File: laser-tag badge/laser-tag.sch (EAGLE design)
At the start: 47 parts, among them J1 JUMPER_SOLDER_1X2_CLOSED, J2 JUMPER_SOLDER_1X2_OPEN, J3 JUMPER_SOLDER_1X2_CLOSED, J4 JUMPER_SOLDER_1X2_CLOSED, J5 JUMPER_SOLDER_1X2_CLOSED, P1 E1260CS021, U1 MKL27Z256VLH4

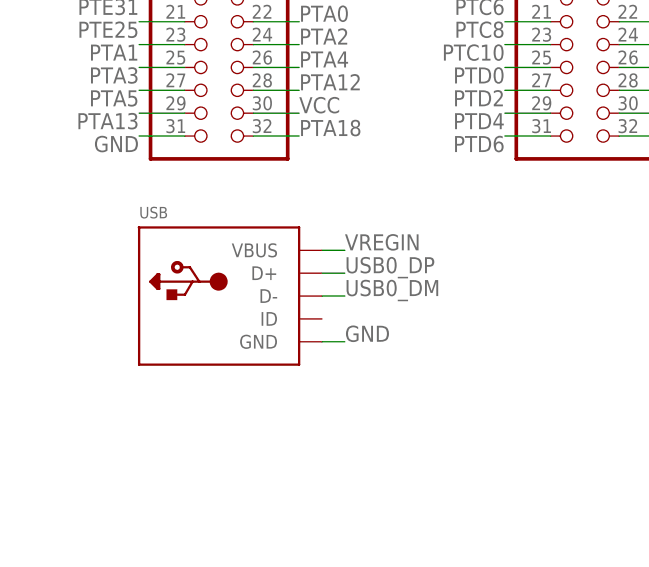
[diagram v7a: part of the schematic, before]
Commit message: Switch to micro-USB connector
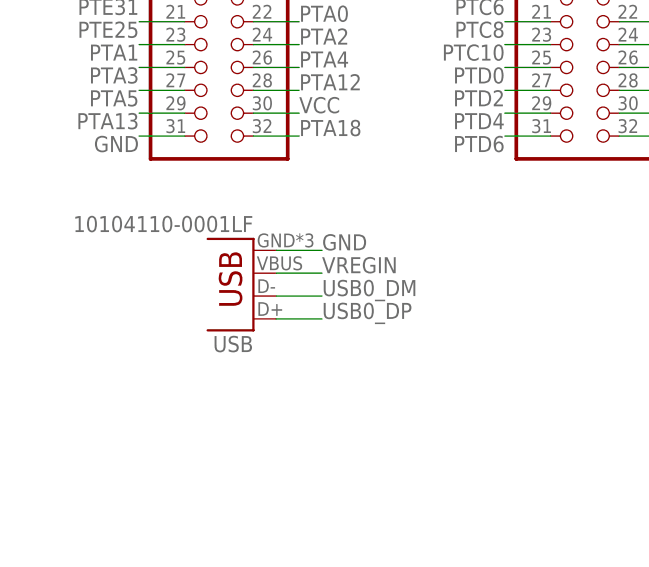
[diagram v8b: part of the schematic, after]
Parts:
- USB: value (none) -> 10104110-0001LF; device adafruit:USBMINIB -> SparkFun-Connectors:USB-MICROB
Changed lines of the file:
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@@
 <layer number="112" name="tSilk" color="7" fill="1" visible="no" active="yes"/>
 <layer number="113" name="ReferenceLS" color="7" fill="1" visible="no" active="no"/>
+<layer number="114" name="Badge_Outline" color="7" fill="1" visible="yes" active="yes"/>
+<layer number="115" name="ReferenceISLANDS" color="7" fill="1" visible="yes" active="yes"/>
 <layer number="116" name="Patch_BOT" color="9" fill="4" visible="no" active="yes"/>
 <layer number="118" name="Rect_Pads" color="7" fill="1" visible="no" active="no"/>
@@
 <part name="R1" library="rcl" deviceset="R-EU_" device="R0603" value="10k"/>
 <part name="GND2" library="supply1" deviceset="GND" device=""/>
-<part name="USB" library="adafruit" deviceset="USB" device="MINIB"/>
 <part name="R2" library="rcl" deviceset="R-EU_" device="R0603" value="10"/>
 <part name="C5" library="rcl" deviceset="C-EU" device="C0603K" value="10 uF"/>
@@
 <part name="R4" library="rcl" deviceset="R-EU_" device="R0603" value="10k"/>
 <part name="BAT2" library="adafruit" deviceset="CR2032" device="SMT" value="BK-883"/>
+<part name="USB" library="SparkFun-Connectors" deviceset="USB" device="-MICROB" value="10104110-0001LF"/>
 </parts>
 <sheets>
@@
 <instance part="R1" gate="G$1" x="-38.1" y="78.74" rot="R90"/>
 <instance part="GND2" gate="1" x="-38.1" y="68.58"/>
-<instance part="USB" gate="G$1" x="-106.68" y="5.08"/>
 <instance part="R2" gate="G$1" x="-17.78" y="86.36" rot="R90"/>
 <instance part="C5" gate="G$1" x="-58.42" y="81.28"/>
@@
 <instance part="R4" gate="G$1" x="-10.16" y="66.04" rot="R90"/>
 <instance part="BAT2" gate="G$1" x="-124.46" y="88.9" rot="R90"/>
+<instance part="USB" gate="G$1" x="-104.14" y="10.16" rot="R180"/>
 </instances>
 <busses>
@@
 </segment>
 <segment>
+<wire x1="-101.6" y1="10.16" x2="-96.52" y2="10.16" width="0.1524" layer="91"/>
+<label x="-96.52" y="10.16" size="1.778" layer="95"/>
 <pinref part="USB" gate="G$1" pin="GND"/>
-<wire x1="-96.52" y1="0" x2="-93.98" y2="0" width="0.1524" layer="91"/>
-<label x="-93.98" y="0" size="1.778" layer="95"/>
 </segment>
 <segment>
@@
 </segment>
 <segment>
+<wire x1="-101.6" y1="2.54" x2="-96.52" y2="2.54" width="0.1524" layer="91"/>
+<label x="-96.52" y="2.54" size="1.778" layer="95"/>
 <pinref part="USB" gate="G$1" pin="D+"/>
-<wire x1="-96.52" y1="7.62" x2="-93.98" y2="7.62" width="0.1524" layer="91"/>
-<label x="-93.98" y="7.62" size="1.778" layer="95"/>
 </segment>
 </net>
@@
 </segment>
 <segment>
+<wire x1="-101.6" y1="5.08" x2="-96.52" y2="5.08" width="0.1524" layer="91"/>
+<label x="-96.52" y="5.08" size="1.778" layer="95"/>
 <pinref part="USB" gate="G$1" pin="D-"/>
-<wire x1="-96.52" y1="5.08" x2="-93.98" y2="5.08" width="0.1524" layer="91"/>
-<label x="-93.98" y="5.08" size="1.778" layer="95"/>
 </segment>
 </net>
@@
 </segment>
 <segment>
+<wire x1="-101.6" y1="7.62" x2="-96.52" y2="7.62" width="0.1524" layer="91"/>
+<label x="-96.52" y="7.62" size="1.778" layer="95"/>
 <pinref part="USB" gate="G$1" pin="VBUS"/>
-<wire x1="-96.52" y1="10.16" x2="-93.98" y2="10.16" width="0.1524" layer="91"/>
-<label x="-93.98" y="10.16" size="1.778" layer="95"/>
-</segment>
-</net>
+</segment>
+</net>
